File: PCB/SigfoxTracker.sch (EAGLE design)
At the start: 41 parts, among them IC1 WSSFM10R1AT, J1 SMA-J-P-H-ST-EM1, Q7 IRLML5203, U1 SIM28ML

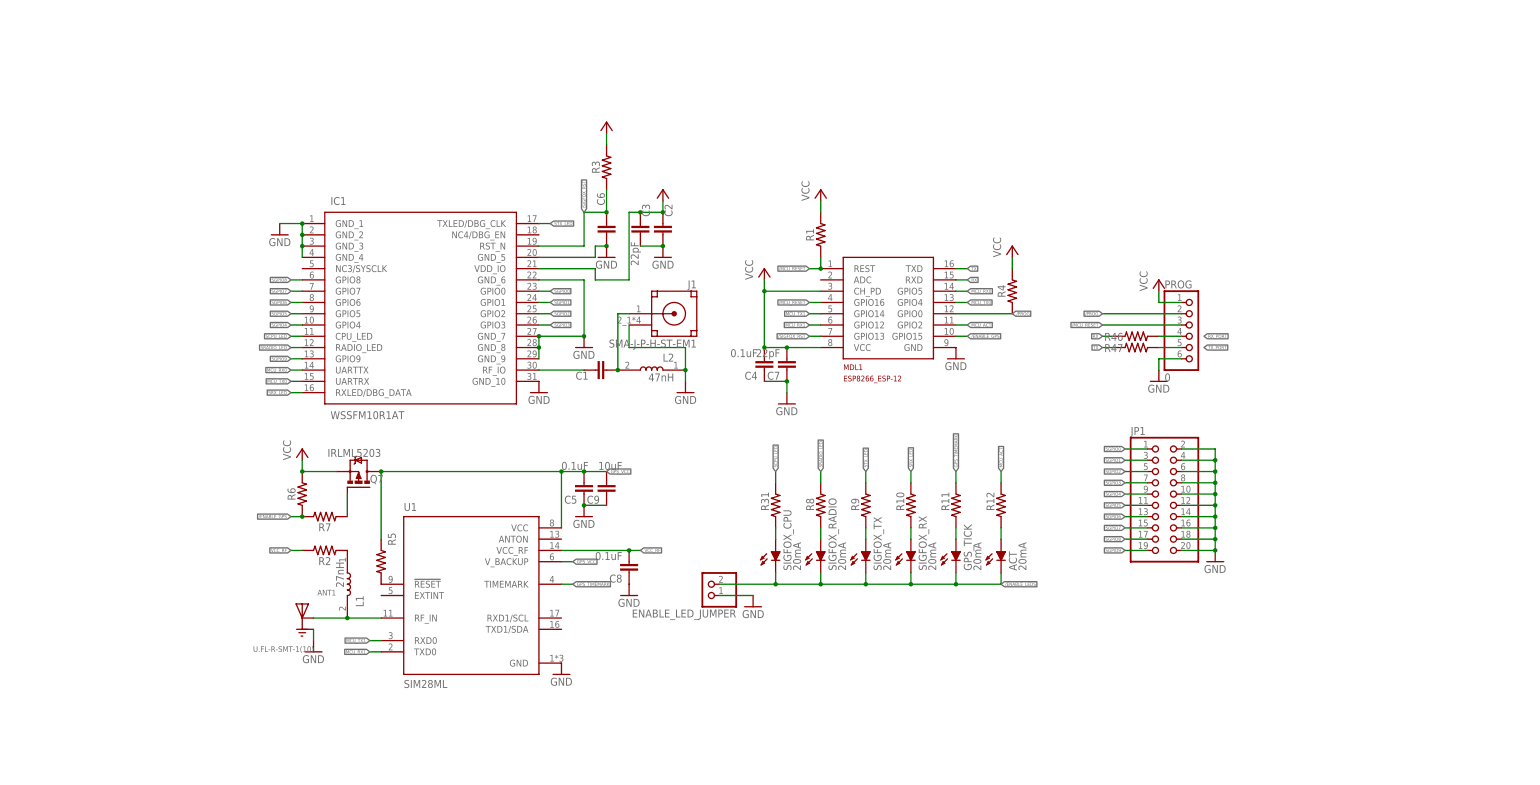
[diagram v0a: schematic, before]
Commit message: More stitching, cleaned up schematic
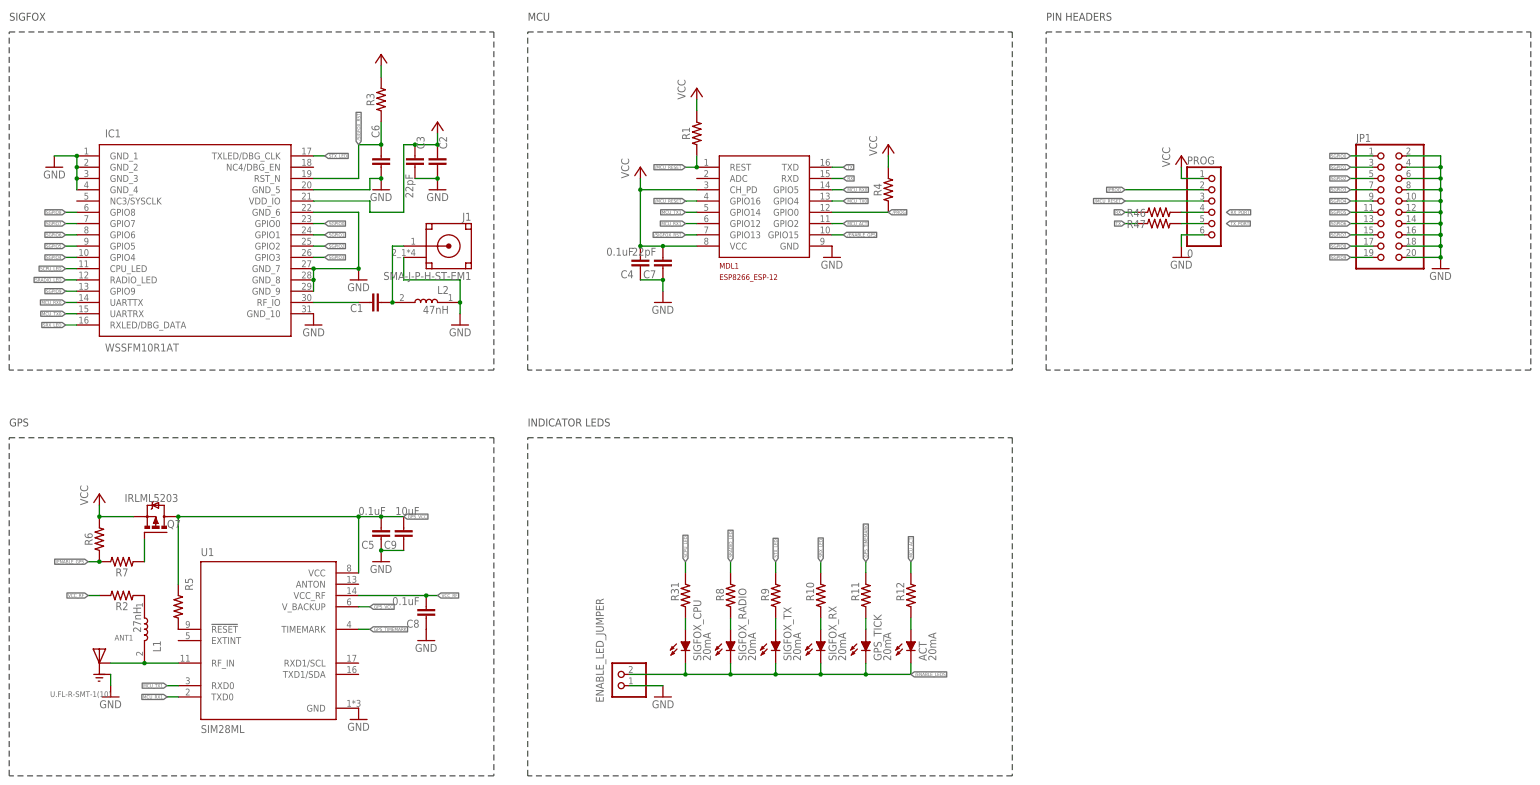
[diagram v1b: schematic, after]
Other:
- note added: "GPS"
- note added: "INDICATOR LEDS"
- note added: "MCU"
- note added: "PIN HEADERS"
- note added: "SIGFOX"
- moved on the sheet: ACT, ANT1, C1, C2, C3, C4, C5, C6, C7, C8, C9, ENABLE_LED_JUMPER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

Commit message: New revision, broken out i2C, ADC input, changed silkscreen
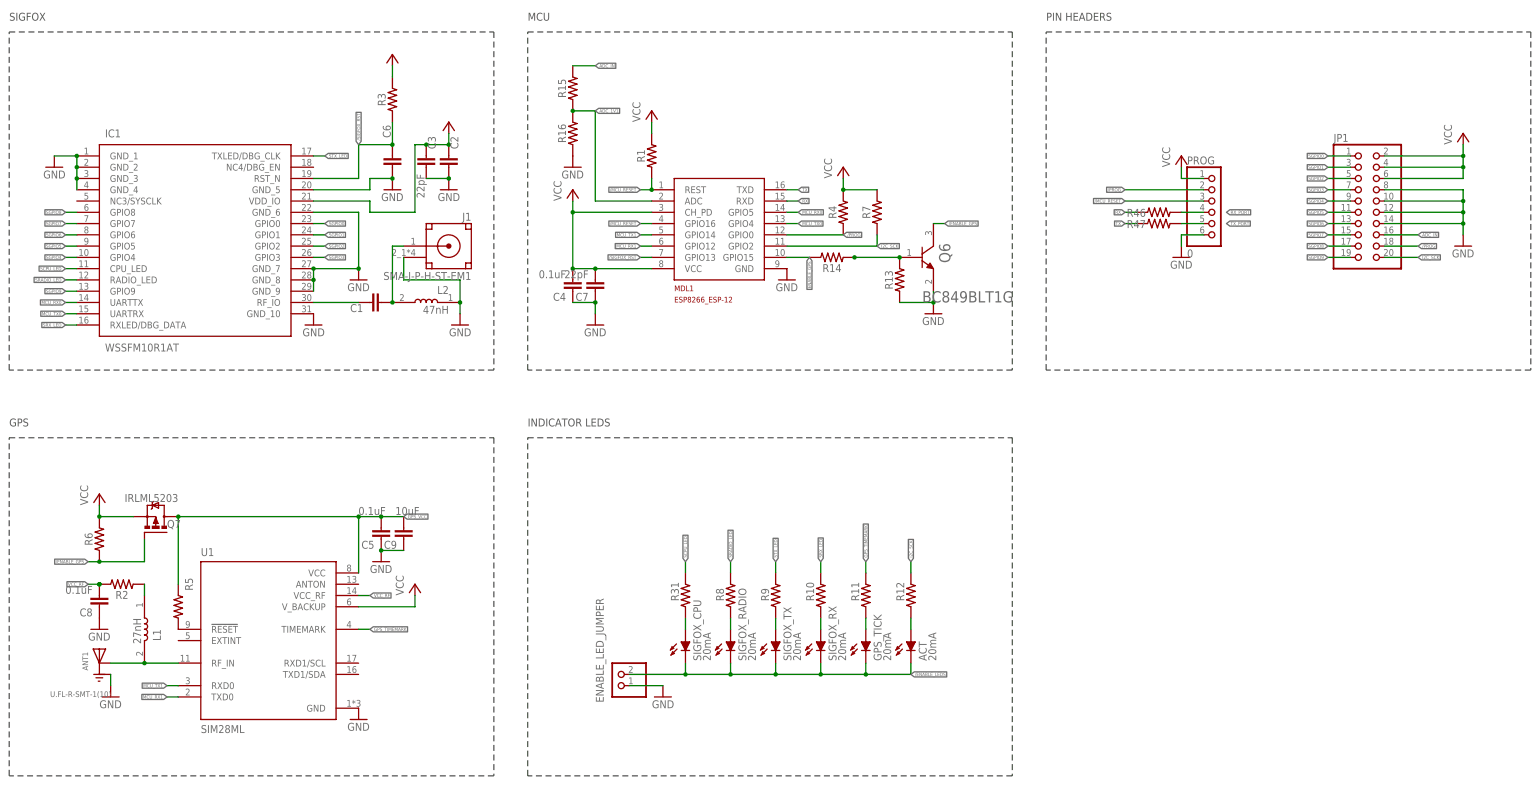
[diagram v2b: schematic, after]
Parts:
- added Q6: ON_SEMICONDUCTOR_BC849BLT1GON_SEMICONDUCTOR_BC849BLT1G_0_0, On Semiconductor - BC849BLT1G:ON_SEMICONDUCTOR_BC849BLT1GON_SEMICONDUCTOR_BC849BLT1G_0_0
- added R13: 100k, ESP32_DMX_Audio:52101-101-REV-A_RC-MASTER-SMD_R_0603MP
- added R14: 1K, ESP32_DMX_Audio:52101-101-REV-A_RC-MASTER-SMD_R_0603MP
- added R15: 10K, ESP32_DMX_Audio:52101-101-REV-A_RC-MASTER-SMD_R_0603MP
- added R16: 3V3, ESP32_DMX_Audio:52101-101-REV-A_RC-MASTER-SMD_R_0603MP
- R4: value 100k -> 4K7
- R7: value 10R -> 4K7; device 52101-101-REV-A:RC-MASTER-SMD_R_0603MP -> ESP32_DMX_Audio:52101-101-REV-A_RC-MASTER-SMD_R_0603MP
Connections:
- removed net MCU_ACT: MDL1.GPIO2, R12.1
- removed net MOS_GATE: Q7.G, R7.1
- new net ADC_1V1: MDL1.ADC, R15.1, R16.2
- new net ADC_IN: JP1.16, R15.2
- new net ENABLE_GPS: MDL1.GPIO15, R14.2
- new net I2C_SCK: JP1.20, MDL1.GPIO2, R12.1, R7.1
- new net N$10: Q6.B, R13.2, R14.1
- net /ENABLE_GPS: now also Q6.C, Q7.G; no longer MDL1.GPIO15, R7.2
- net /PROG: now also JP1.18
- net GND: now also Q6.E, R13.1, R16.1; no longer JP1.16, JP1.18, JP1.2, JP1.20, JP1.4, JP1.6
- net GPS_VCC: no longer U1.V_BACKUP
- net VCC: now also JP1.2, JP1.4, JP1.6, R7.2, U1.V_BACKUP
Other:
- moved on the sheet: C2, C3, C4, C6, C7, C8, JP1, MDL1, R1, R2, R3, R4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
